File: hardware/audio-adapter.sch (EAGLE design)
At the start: 21 parts

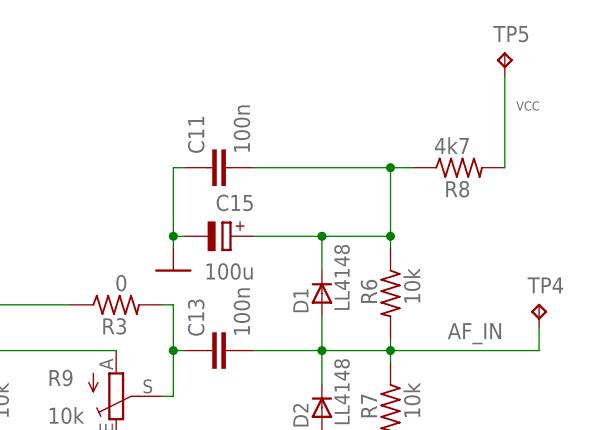
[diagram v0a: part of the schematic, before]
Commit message: - T-TWR PLUS V2.0 MOD board support added
- ESP32S3 -> ESP32E adapter Rev.C added
- AudioAdapter BOM fix (4k7->33k)
- README.md updated
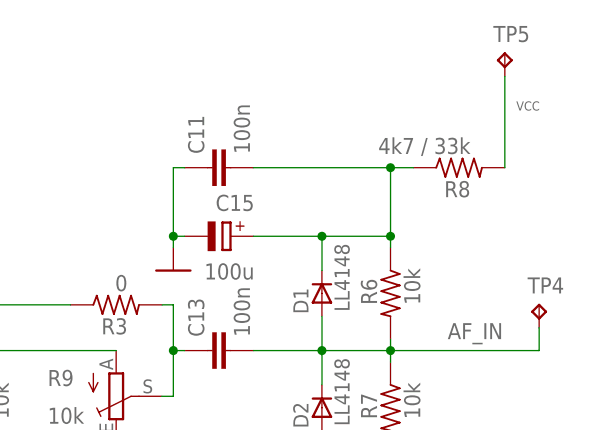
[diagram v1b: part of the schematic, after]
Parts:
- R8: value 4k7 -> 4k7 / 33k
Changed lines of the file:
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@@
 <part name="R6" library="resistor" deviceset="R-US_" device="R0805" value="10k"/>
 <part name="R7" library="resistor" deviceset="R-US_" device="R0805" value="10k"/>
-<part name="R8" library="resistor" deviceset="R-US_" device="R0805" value="4k7"/>
+<part name="R8" library="resistor" deviceset="R-US_" device="R0805" value="4k7 / 33k"/>
 <part name="C11" library="resistor" deviceset="C-EU" device="C0805" value="100n"/>
 <part name="D1" library="_hhn_diodes_smd" deviceset="LL4148" device=""/>
